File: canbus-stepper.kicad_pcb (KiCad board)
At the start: 2 copper layers, 40.3 x 40.3 mm, 64 parts, among them J1 TYPE-C USB SOCKET, J2 Motor Output, J3 CAN Daisy-Chain 1, J4 CAN Daisy-Chain 2, J5 Qwiic I2C, J6 AUX Port, J7 SFV30R-2STBE1HLF (30-Pin OLED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, J8 24V Power Input Terminal, J9 24V Power Output Terminal, Q1 AO4407A, SW1 SW_Push, SW2 SW_Push, SW3 SW_Push, SW4 SW_Push, U1 ESP32-S3-WROOM-1, U2 TMC2209, U3 AS5600-ASOT, U4 TCAN1051VDRBTQ1, U5 MP2315, U6 AP2112K-3.3TRG1, U7 USBLC6-2SC6

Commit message: style: arrange unplaced PCB components into 8 functional matrix groups outside board boundary
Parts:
- moved D5 68.7 mm to (236.0, 150.0)
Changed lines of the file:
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@@
 	(footprint "Package_TO_SOT_SMD:SOT-23"
 		(layer "F.Cu")
-		(at 199.168654 91.987308)
+		(at 236.00 150.00)
 		(descr "SOT, 3 Pin (JEDEC TO-236 Var AB https://www.jedec.org/document_search?search_api_views_fulltext=TO-236)")
 		(tags "SOT TO_SOT_SMD")

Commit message: fix: resolve D5 SOD-123 footprint, add F1/F2 fuse net wiring, and map thermal/shield pads for ESP32, TCAN1051, J2, J8, J9, SW1-SW4 to eliminate all warnings and errors
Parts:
- D3: moved to B.Cu
- D5: footprint Package_TO_SOT_SMD:SOT-23 -> Diode_SMD:D_SOD-123
- moved U4 11.3 mm to (157.8, 107.8), turned to 90 degrees
- moved U5 9.37 mm to (161.9, 104.9), turned to 0 degrees
- moved U6 7.69 mm to (166.6, 104.9)
- moved F1 5.60 mm to (179.0, 94.0)
- moved D3 0.76 mm to (166.1, 105.8)
- moved R1 0.66 mm to (140.8, 107.5)
- moved R2 0.66 mm to (148.8, 107.5)
- moved SW1 0.66 mm to (144.8, 107.6)
- moved SW2 0.66 mm to (152.8, 107.6)

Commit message: fix: connect J8 24V input and J1 USB VBUS to fuse nets F1 and F2
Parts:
- moved F1 0.81 mm to (179.6, 93.5)
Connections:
- D4 pad 3: unconnected-(D4-GND-Pad3) -> GND
- F1 pad 1: unconnected-(F1-~-Pad1) -> /+24V_IN
- F1 pad 2: unconnected-(F1-~-Pad2) -> /+24V_FUSED
- J2 pad 1: /MOTOR_OA1 -> unconnected-(J2-Pin_1-Pad1)
- J2 pad 2: /MOTOR_OA2 -> unconnected-(J2-Pin_2-Pad2)
- J2 pad 3: /MOTOR_OB1 -> unconnected-(J2-Pin_3-Pad3)
- J2 pad 4: /MOTOR_OB2 -> unconnected-(J2-Pin_4-Pad4)
- J2 pad MP: unconnected-(J2-PadMP) -> (no net)
- J3 pad 1: VBUS -> unconnected-(J3-Pin_1-Pad1)
- J3 pad 2: GND -> unconnected-(J3-Pin_2-Pad2)
- J3 pad 3: /CANH -> unconnected-(J3-Pin_3-Pad3)
- J3 pad 4: /CANL -> unconnected-(J3-Pin_4-Pad4)
- J3 pad MP: unconnected-(J3-PadMP) -> (no net)
- J4 pad 1: VBUS -> unconnected-(J4-Pin_1-Pad1)
- J4 pad 2: GND -> unconnected-(J4-Pin_2-Pad2)
- J4 pad 3: /CANH -> unconnected-(J4-Pin_3-Pad3)
- J4 pad 4: /CANL -> unconnected-(J4-Pin_4-Pad4)
- J4 pad MP: unconnected-(J4-PadMP) -> (no net)
- J5 pad 1: GND -> unconnected-(J5-Pin_1-Pad1)
- J5 pad 2: +3V3 -> unconnected-(J5-Pin_2-Pad2)
- J5 pad 3: /SDA -> unconnected-(J5-Pin_3-Pad3)
- J5 pad 4: /SCL -> unconnected-(J5-Pin_4-Pad4)
- J5 pad MP: unconnected-(J5-PadMP) -> (no net)
- J6 pad 1: GND -> unconnected-(J6-Pin_1-Pad1)
- J6 pad 2: +3V3 -> unconnected-(J6-Pin_2-Pad2)
- J6 pad 3: /AUX1 -> unconnected-(J6-Pin_3-Pad3)
- J6 pad 4: /AUX2 -> unconnected-(J6-Pin_4-Pad4)
- J6 pad MP: unconnected-(J6-PadMP) -> (no net)
- J8 pad 3: (no net) -> Net-(J8-SH-Pad3)
- J8 pad 4: (no net) -> Net-(J8-SH-Pad3)
- J9 pad 3: (no net) -> Net-(J9-SH-Pad3)
- J9 pad 4: (no net) -> Net-(J9-SH-Pad3)
- SW1 pad 2: GND -> unconnected-(SW1-Pad2)
- SW2 pad 2: GND -> unconnected-(SW2-Pad2)
- SW3 pad 1: /SW1 -> unconnected-(SW3-Pad1)
- SW3 pad 2: GND -> unconnected-(SW3-Pad2)
- SW4 pad 1: /SW2 -> unconnected-(SW4-Pad1)
- SW4 pad 2: GND -> unconnected-(SW4-Pad2)
- U1 pad 42: (no net) -> GND
- U1 pad 43: (no net) -> GND
- U1 pad 44: (no net) -> GND
- U1 pad 45: (no net) -> GND
- U1 pad 46: (no net) -> GND
- U1 pad 47: (no net) -> GND
- U1 pad 48: (no net) -> GND
- U1 pad 49: (no net) -> GND
- U1 pad 50: (no net) -> GND
- U1 pad 51: (no net) -> GND
- U1 pad 52: (no net) -> GND
- U1 pad 53: (no net) -> GND
- U1 pad 54: (no net) -> GND
- U1 pad 55: (no net) -> GND
- U1 pad 56: (no net) -> GND
- U1 pad 57: (no net) -> GND
- U1 pad 58: (no net) -> GND
- U1 pad 59: (no net) -> GND
- U1 pad 60: (no net) -> GND
- U1 pad 61: (no net) -> GND
- U1 pad 61_1: (no net) -> GND
- U1 pad 61_2: (no net) -> GND
- U1 pad 61_3: (no net) -> GND
- U1 pad 61_4: (no net) -> GND
- U1 pad 61_5: (no net) -> GND
- U1 pad 61_6: (no net) -> GND
- U1 pad 61_7: (no net) -> GND
- U1 pad 61_8: (no net) -> GND
- U1 pad 62: (no net) -> GND
- U1 pad 63: (no net) -> GND
- U1 pad 64: (no net) -> GND
- U1 pad 65: (no net) -> GND
- U4 pad 9: (no net) -> unconnected-(U4-GND-Pad9)

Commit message: chore: save board and schematic progress before autoplacer development
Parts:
- added SW5: Termination, CANBUS-Stepper:SW_TS31-46-35-BK-B-160-RA-SMT-TR, F.Cu at (178.9, 109.2)
- U1: value ESP32-S3-WROOM-1 -> ESP32-S3-MINI-1
- moved F1 1.12 mm to (180.1, 94.5)
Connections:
- U1 pad 10: /TMC_TX -> /DIR
- U1 pad 11: /TMC_RX -> /NTC_SENSE
- U1 pad 13: /USB_D- -> /SCL
- U1 pad 14: /USB_D+ -> /LED1
- U1 pad 15: unconnected-(U1-NC-Pad15) -> /INDEX
- U1 pad 16: /IO46 -> GND
- U1 pad 17: /SCL -> /LED2
- U1 pad 18: /LED1 -> /AUX2
- U1 pad 19: /INDEX -> /AUX1
- U1 pad 2: +3V3 -> (no net)
- U1 pad 20: /LED2 -> (no net)
- U1 pad 21: /AUX2 -> /DIAG
- U1 pad 22: /AUX1 -> /TMC_TX
- U1 pad 23: /TMC_EN -> /TMC_RX
- U1 pad 24: /CAN_RX -> /USB_D-
- U1 pad 25: /CAN_TX -> /USB_D+
- U1 pad 26: unconnected-(U1-NC-Pad26) -> /TMC_EN
- U1 pad 27: /IO0 -> (no net)
- U1 pad 28: /SW1 -> /CAN_RX
- U1 pad 29: /SW2 -> (no net)
- U1 pad 3: /EN -> +3V3
- U1 pad 30: /CAN_STB -> (no net)
- U1 pad 31: /DISABLE_3V3 -> /CAN_TX
- U1 pad 32: unconnected-(U1-NC-Pad32) -> (no net)
- U1 pad 33: unconnected-(U1-NC-Pad33) -> (no net)
- U1 pad 34: unconnected-(U1-NC-Pad34) -> (no net)
- U1 pad 35: unconnected-(U1-NC-Pad35) -> /SW1
- U1 pad 36: unconnected-(U1-NC-Pad36) -> /SW2
- U1 pad 37: unconnected-(U1-NC-Pad37) -> /CAN_STB
- U1 pad 38: unconnected-(U1-NC-Pad38) -> /DISABLE_3V3
- U1 pad 39: unconnected-(U1-NC-Pad39) -> /EN
- U1 pad 4: /VBUS_SENSE -> /IO0
- U1 pad 40: GND -> unconnected-(U1-NC-Pad40)
- U1 pad 41: GND -> unconnected-(U1-NC-Pad41)
- U1 pad 46: GND -> /IO46
- U1 pad 5: /STEP -> (no net)
- U1 pad 6: /DIR -> (no net)
- U1 pad 7: /NTC_SENSE -> (no net)
- U1 pad 8: unconnected-(U1-NC-Pad8) -> /VBUS_SENSE
- U1 pad 9: /DIAG -> /STEP
- U2 pad 10: /MS2 -> GND
- U2 pad 9: /MS1 -> GND
- U3 pad 2: /ENC_OUT_P -> GND
- U3 pad 3: /ENC_OUT_N -> /ENC_OUT_P
- U3 pad 5: GND -> /ENC_OUT_N
- U3 pad 6: /SCL -> /SDA
- U3 pad 7: /SDA -> /SCL
- U4 pad 3: +3V3 -> +5V
- U4 pad 5: /CAN_VREF -> +3V3
- U6 pad 4: +3V3 -> unconnected-(U6-NC-Pad4)
- U6 pad 5: unconnected-(U6-NC-Pad5) -> +3V3

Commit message: update canbus ohm sw footprint
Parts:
- SW5: footprint CANBUS-Stepper:SW_TS31-46-35-BK-B-160-RA-SMT-TR -> Button_Switch_SMD:SW_DIP_SPSTx01_Slide_Copal_CHS-01A_W5.08mm_P1.27mm_JPin

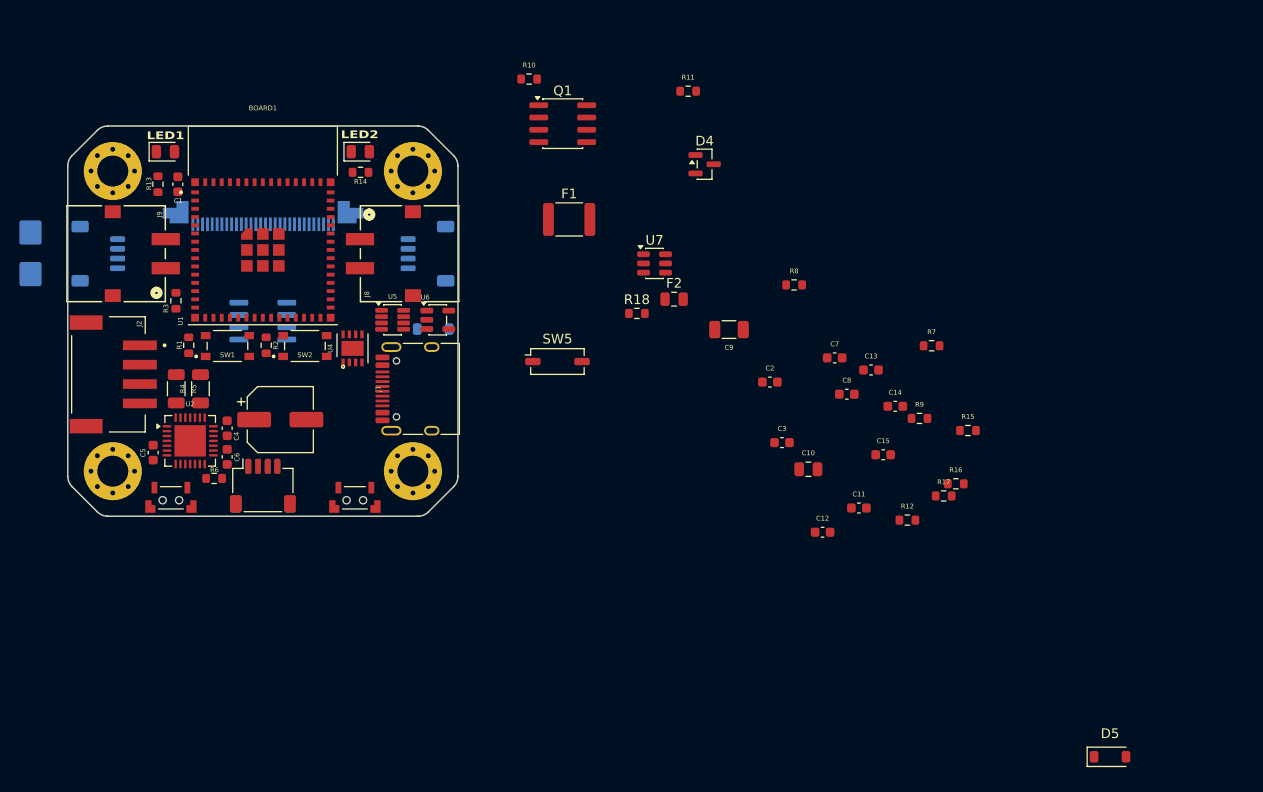
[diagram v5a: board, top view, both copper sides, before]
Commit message: full revision of net connection, components
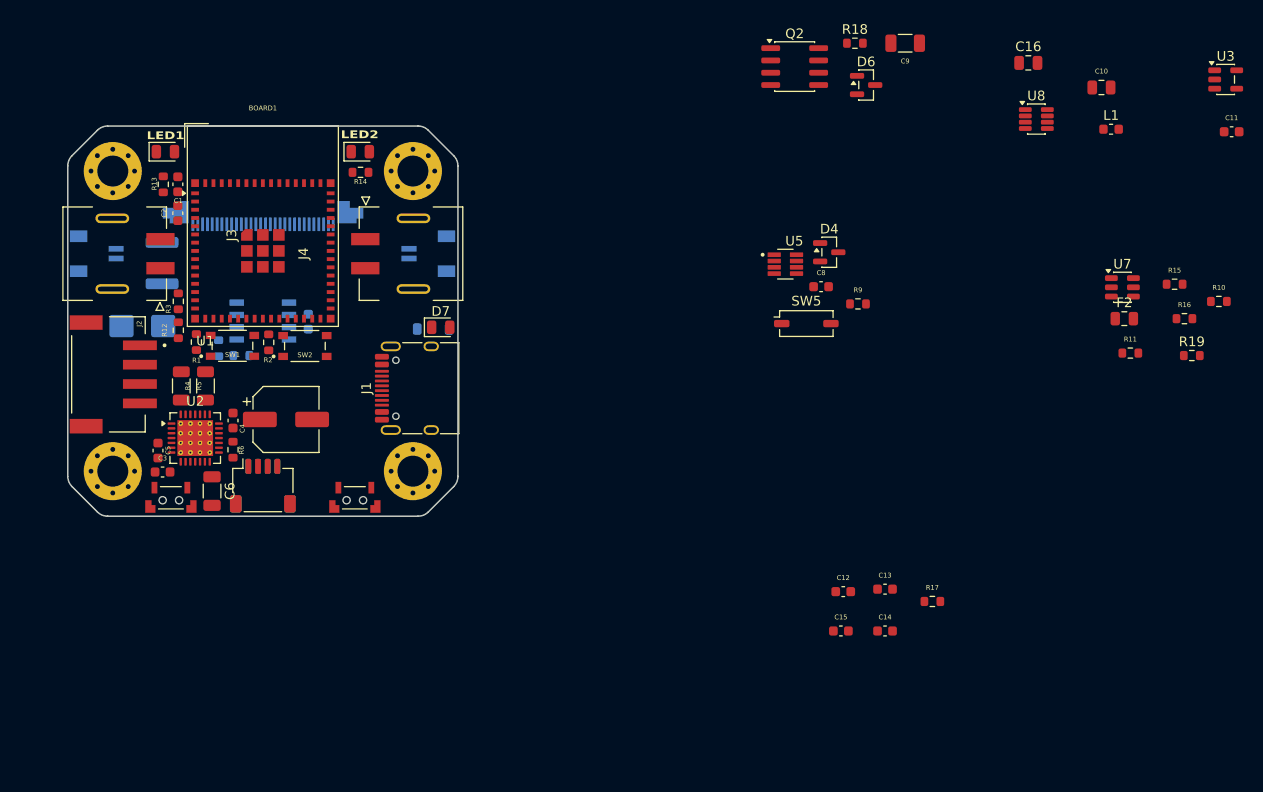
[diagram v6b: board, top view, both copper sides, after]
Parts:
- removed D5: BZX84C12V, Diode_SMD:D_SOD-123
- removed J8: 24V Power Input Terminal, CANBUS-Stepper:CONN_SD-43650-005_02_MOL
- removed J9: 24V Power Output Terminal, CANBUS-Stepper:CONN_SD-43650-005_02_MOL
- removed Q1: AO4407A, Package_SO:SOIC-8_3.9x4.9mm_P1.27mm
- removed U4: TCAN1051VDRBTQ1, CANBUS-Stepper:TCAN1051VDRBTQ1
- removed U6: AP2112K-3.3TRG1, Package_TO_SOT_SMD:SOT-23-5
- added C16: 1uF, Capacitor_SMD:C_0805_2012Metric, F.Cu at (227.6, 78.3)
- added D6: BZX84Cxx, Package_TO_SOT_SMD:SOT-23, F.Cu at (210.8, 80.6)
- added D7: LED, LED_SMD:LED_0805_2012Metric, F.Cu at (166.9, 105.6)
- added IC1: AS5600-ASOT, CANBUS-Stepper:AS5600-ASOT, B.Cu at (148.5, 105.0)
- added J10: SM02B-SRSS-TB_LF__SN_, CANBUS-Stepper:SM02B-SRSS-TB_LF__SN_, B.Cu at (131.4, 98.0)
- added J11: SM02B-SRSS-TB_LF__SN_, CANBUS-Stepper:SM02B-SRSS-TB_LF__SN_, B.Cu at (165.6, 98.0)
- added L1: 4.7uH, Inductor_SMD:L_0603_1608Metric, F.Cu at (236.1, 85.2)
- added Q2: FDS9435A, Package_SO:SOIC-8_3.9x4.9mm_P1.27mm, F.Cu at (203.4, 78.7)
- added R19: 1k, Resistor_SMD:R_0603_1608Metric, F.Cu at (244.4, 108.6)
- added U8: MP2315GJ, Package_TO_SOT_SMD:SOT-23-8, F.Cu at (228.4, 84.1)
- C6: value 100nF -> 10uF 50V; footprint Capacitor_SMD:C_0603_1608Metric -> Capacitor_SMD:C_1206_3216Metric
- C7, F1, R7, R8: moved to B.Cu
- J1: value TYPE-C USB SOCKET -> USB_C_Receptacle_USB2.0_16P
- J3: value CAN Daisy-Chain 1 -> 436500209; footprint Connector_JST:JST_SH_SM04B-SRSS-TB_1x04-1MP_P1.00mm_Horizontal -> CANBUS-Stepper:MOLEX_436500209; moved to F.Cu
- J4: value CAN Daisy-Chain 2 -> 436500209; footprint Connector_JST:JST_SH_SM04B-SRSS-TB_1x04-1MP_P1.00mm_Horizontal -> CANBUS-Stepper:MOLEX_436500209; moved to F.Cu
- U1: footprint CANBUS-Stepper:XCVR_ESP32-S3-MINI-1-N4R2 -> RF_Module:ESP32-S2-MINI-1
- U2: value TMC2209 -> TMC2209-LA; footprint Package_DFN_QFN:QFN-28-1EP_5x5mm_P0.5mm_EP3.25x3.25mm -> Package_DFN_QFN:VQFN-28-1EP_5x5mm_P0.5mm_EP3.7x3.7mm_ThermalVias
- U3: value AS5600-ASOT -> AP2112K-3.3; footprint Package_SO:SOIC-8_3.9x4.9mm_P1.27mm -> Package_TO_SOT_SMD:SOT-23-5; moved to F.Cu
- U5: value MP2315 -> TCAN1044VDDFRQ1; footprint Package_TO_SOT_SMD:SOT-23-8 -> CANBUS-Stepper:SOT65P280X110-8N
- moved U3 102.5 mm to (247.9, 80.0), turned to 0 degrees
- moved R12 77.8 mm to (139.8, 105.9), turned to 90 degrees
- moved R10 74.9 mm to (247.2, 103.0)
- moved R7 71.3 mm to (146.3, 108.6), turned to 180 degrees
- moved C3 64.0 mm to (138.1, 120.6)
- moved C2 63.6 mm to (139.7, 93.8), turned to 90 degrees
- moved R8 59.8 mm to (143.9, 107.8), turned to 90 degrees
- moved C11 54.7 mm to (248.6, 85.4)
- moved C7 54.5 mm to (153.2, 105.1), turned to -90 degrees
- moved R11 53.1 mm to (238.1, 108.3)
- moved C10 49.7 mm to (235.1, 80.9)
- moved U7 48.4 mm to (237.3, 101.5)
- moved F2 46.5 mm to (237.5, 104.7)
- moved F1 42.3 mm to (138.1, 99.0), turned to -90 degrees
- moved U5 41.0 mm to (202.5, 99.1)
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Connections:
- net /LED1_K renamed Net-(D1-A)
- net /LED2_K renamed Net-(D2-A)
- C3 pad 1: VBUS -> /VCP
- C3 pad 2: GND -> /+24V_FUSED
- C4 pad 1: VBUS -> /TMC_5VOUT
- C6 pad 1: +3V3 -> /+24V_FUSED
- C8 pad 1: +3V3 -> +5V
- C9 pad 1: VBUS -> /VBUS
- C_BULK1 pad 1: VBUS -> /VBUS
- D3 pad 1: +5V -> /USB_VBUS
- D3 pad 2: /USB_VBUS -> /USB_VBUS_FUSED
- D4 pad 1: unconnected-(D4-CANH-Pad1) -> /CANH
- D4 pad 2: unconnected-(D4-CANL-Pad2) -> /CANL
- F1 pad 1: /+24V_IN -> /+24V_RAW
- F2 pad 1: unconnected-(F2-~-Pad1) -> /USB_VBUS_RAW
- F2 pad 2: unconnected-(F2-~-Pad2) -> /USB_VBUS_FUSED
- J1 pad A1: /USB_VBUS -> GND
- J1 pad A12: /USB_VBUS -> GND
- J1 pad A4: GND -> /USB_VBUS_RAW
- J1 pad A6: /USB_CC2 -> /USB_D+
- J1 pad A9: GND -> /USB_VBUS_RAW
- J1 pad B1: /USB_VBUS -> GND
- J1 pad B12: /USB_VBUS -> GND
- J1 pad B4: GND -> /USB_VBUS_RAW
- J1 pad B5: /USB_D+ -> /USB_CC2
- J1 pad B6: /USB_D- -> /USB_D+
- J1 pad B7: /USB_D+ -> /USB_D-
- J1 pad B9: GND -> /USB_VBUS_RAW
- J1 pad SH: unconnected-(J1-Shield-PadSH) -> GND
- J2 pad 1: unconnected-(J2-Pin_1-Pad1) -> /MOTOR_OA1
- J2 pad 2: unconnected-(J2-Pin_2-Pad2) -> /MOTOR_OA2
- J2 pad 3: unconnected-(J2-Pin_3-Pad3) -> /MOTOR_OB1
- J2 pad 4: unconnected-(J2-Pin_4-Pad4) -> /MOTOR_OB2
- J3 pad 1: unconnected-(J3-Pin_1-Pad1) -> /+24V_RAW
- J3 pad 2: unconnected-(J3-Pin_2-Pad2) -> GND
- J4 pad 1: unconnected-(J4-Pin_1-Pad1) -> /+24V_RAW
- J4 pad 2: unconnected-(J4-Pin_2-Pad2) -> GND
- J5 pad 1: unconnected-(J5-Pin_1-Pad1) -> GND
- J5 pad 2: unconnected-(J5-Pin_2-Pad2) -> +3V3
- J5 pad 3: unconnected-(J5-Pin_3-Pad3) -> /SDA
- J5 pad 4: unconnected-(J5-Pin_4-Pad4) -> /SCL
- J6 pad 1: unconnected-(J6-Pin_1-Pad1) -> GND
- J6 pad 2: unconnected-(J6-Pin_2-Pad2) -> +3V3
- J6 pad 3: unconnected-(J6-Pin_3-Pad3) -> /AUX1
- J6 pad 4: unconnected-(J6-Pin_4-Pad4) -> /AUX2
- J7 pad 1: unconnected-(J7-Pin_1-Pad1) -> GND
- J7 pad 18: GND -> +3V3
- R10 pad 1: VBUS -> /USB_VBUS_FUSED
- R18 pad 1: unconnected-(R18-~-Pad1) -> /GATE_24V
- R18 pad 2: unconnected-(R18-~-Pad2) -> GND
- SW1 pad 2: unconnected-(SW1-Pad2) -> GND
- SW2 pad 2: unconnected-(SW2-Pad2) -> GND
- SW3 pad 1: unconnected-(SW3-Pad1) -> /SW1
- SW3 pad 2: unconnected-(SW3-Pad2) -> GND
- SW4 pad 1: unconnected-(SW4-Pad1) -> /SW2
- SW4 pad 2: unconnected-(SW4-Pad2) -> GND
- TVS1 pad 1: VBUS -> /+24V_FUSED
- U1 pad 16: GND -> /LED2
- U1 pad 17: /LED2 -> /AUX2
- U1 pad 18: /AUX2 -> /AUX1
- U1 pad 19: /AUX1 -> unconnected-(U1-IO15-Pad19)
- U1 pad 2: (no net) -> GND
- U1 pad 20: (no net) -> /DIAG
- U1 pad 21: /DIAG -> /TMC_TX
- U1 pad 22: /TMC_TX -> /TMC_RX
- U1 pad 23: /TMC_RX -> /USB_D-
- U1 pad 24: /USB_D- -> /USB_D+
- U1 pad 25: /USB_D+ -> /TMC_EN
- U1 pad 26: /TMC_EN -> unconnected-(U1-IO26-Pad26)
- U1 pad 27: (no net) -> /CAN_RX
- U1 pad 28: /CAN_RX -> unconnected-(U1-IO33-Pad28)
- U1 pad 29: (no net) -> unconnected-(U1-IO34-Pad29)
- U1 pad 30: (no net) -> /CAN_TX
- U1 pad 31: /CAN_TX -> /SW1
- U1 pad 32: (no net) -> /SW2
- U1 pad 33: (no net) -> /CAN_STB
- U1 pad 34: (no net) -> /DISABLE_3V3
- U1 pad 35: /SW1 -> unconnected-(U1-IO39-Pad35)
- U1 pad 36: /SW2 -> unconnected-(U1-IO40-Pad36)
- U1 pad 37: /CAN_STB -> unconnected-(U1-IO41-Pad37)
- U1 pad 38: /DISABLE_3V3 -> unconnected-(U1-IO42-Pad38)
- U1 pad 39: /EN -> unconnected-(U1-TXD0-Pad39)
- U1 pad 44: GND -> /IO46
- U1 pad 45: GND -> /EN
- U1 pad 46: /IO46 -> GND
- U1 pad 5: (no net) -> unconnected-(U1-IO1-Pad5)
- U1 pad 6: (no net) -> unconnected-(U1-IO2-Pad6)
- U1 pad 7: (no net) -> unconnected-(U1-IO3-Pad7)
- U2 pad 11: GND -> /DIAG
- U2 pad 12: /DIAG -> /INDEX
- U2 pad 13: /INDEX -> GND
- U2 pad 14: unconnected-(U2-NC-Pad14) -> /TMC_RX
- U2 pad 15: /TMC_RX -> +3V3
- U2 pad 16: +3V3 -> /STEP
- U2 pad 17: /STEP -> +3V3
- U2 pad 18: /DIR -> GND
- U2 pad 19: VBUS -> /DIR
- U2 pad 20: /BRA -> GND
- U2 pad 21: /MOTOR_OA1 -> /MOTOR_OA2
- U2 pad 22: /MOTOR_OA2 -> /+24V_FUSED
- U2 pad 23: GND -> /BRA
- U2 pad 24: unconnected-(U2-NC-Pad24) -> /MOTOR_OA1
- U2 pad 26: unconnected-(U2-NC-Pad26) -> /MOTOR_OB1
- U2 pad 27: unconnected-(U2-NC-Pad27) -> /BRB
- U2 pad 28: unconnected-(U2-NC-Pad28) -> /+24V_FUSED
- U2 pad 3: /BRB -> GND
- U2 pad 4: /MOTOR_OB1 -> /CPO
- U2 pad 5: /VCP -> /CPI
- U2 pad 6: /CPI -> /VCP
- U2 pad 7: /CPO -> unconnected-(U2-SPREAD-Pad7)
- U3 pad 1: +3V3 -> +5V
- U3 pad 3: /ENC_OUT_P -> +5V
- U3 pad 4: GND -> unconnected-(U3-NC-Pad4)
- U3 pad 5: /ENC_OUT_N -> +3V3
- U5 pad 1: VBUS -> /CAN_TX
- U5 pad 2: /BUCK_SW -> GND
- U5 pad 3: GND -> +5V
- U5 pad 4: /BUCK_BST -> /CAN_RX
- U5 pad 5: VBUS -> +3V3
- U5 pad 6: GND -> /CANL
- U5 pad 7: /BUCK_FB -> /CANH
- U5 pad 8: unconnected-(U5-NC-Pad8) -> /CAN_STB
- U7 pad 1: unconnected-(U7-I/O1-Pad1) -> /USB_D-
- U7 pad 2: unconnected-(U7-GND-Pad2) -> GND
- U7 pad 3: unconnected-(U7-I/O2-Pad3) -> /USB_D+
- U7 pad 4: unconnected-(U7-I/O2-Pad4) -> /MCU_USB_D_P
- U7 pad 5: unconnected-(U7-VBUS-Pad5) -> /USB_VBUS_FUSED
- U7 pad 6: unconnected-(U7-I/O1-Pad6) -> /MCU_USB_D_N
